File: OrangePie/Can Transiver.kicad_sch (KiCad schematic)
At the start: 0 parts

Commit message: Add usb hub and can tranceiver
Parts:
- added C18, C19: 100nF, Capacitor_SMD:C_0402_1005Metric, symbol Device:C_Small
- added R8: 10k, Resistor_SMD:R_0402_1005Metric, symbol Device:R_Small
- added U4: TJA1044GTK_3Z, Package_SON:HVSON-8-1EP_3x3mm_P0.65mm_EP1.6x2.4mm, symbol TJA1044GTK_3Z:TJA1044GTK_3Z
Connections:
- new net: R8.2, U4.8 (STB)
- new net +3V3: C19.2, U4.5 (VIO)
- new net +5V: C18.2, U4.3 (VCC)
- new net CAN_TR.RXD: U4.4 (RXD)
- new net CAN_TR.TXD: U4.1 (TXD)
- new net CAN_TR_OUT.+: U4.7 (CANH)
- new net CAN_TR_OUT.-: U4.6 (CANL)
- new net GND: C18.1, C19.1, R8.1, U4.2 (GND), U4.9 (EP)

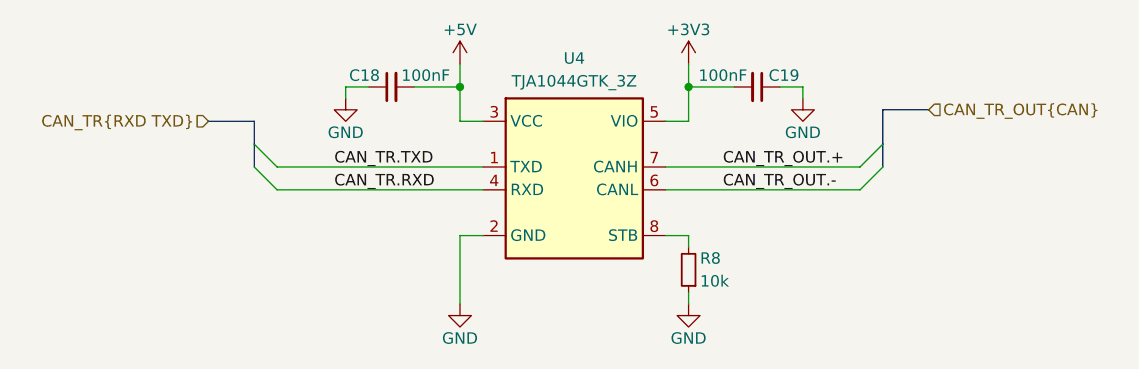
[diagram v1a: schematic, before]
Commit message: Update rest of schematic
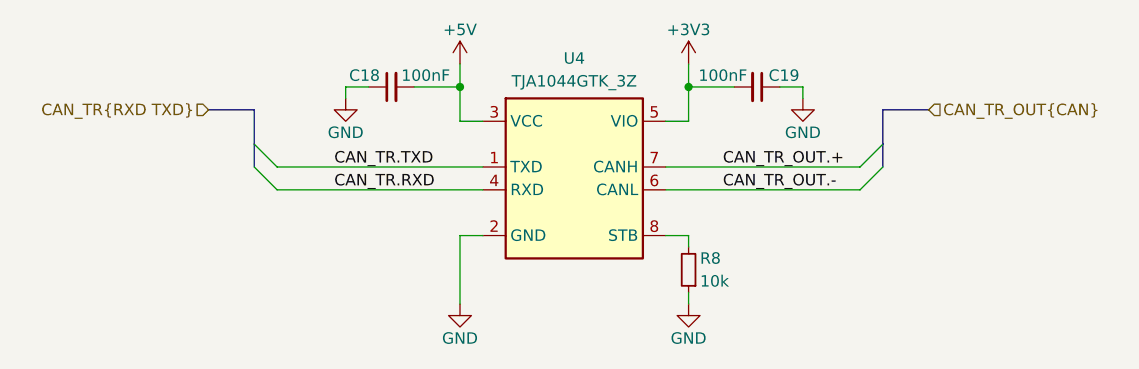
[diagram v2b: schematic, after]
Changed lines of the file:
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@@
 	(bus
 		(pts
-			(xy 96.52 95.25) (xy 101.6 95.25)
+			(xy 96.52 93.98) (xy 101.6 93.98)
 		)
 		(stroke
@@
 	(bus
 		(pts
-			(xy 101.6 95.25) (xy 101.6 97.79)
+			(xy 101.6 93.98) (xy 101.6 97.79)
 		)
 		(stroke
@@
 	(hierarchical_label "CAN_TR{RXD TXD}"
 		(shape input)
-		(at 96.52 95.25 180)
+		(at 96.52 93.98 180)
 		(fields_autoplaced yes)
 		(effects
@@
 					(unit 1)
 				)
+				(path "/3103c9de-f1ba-4d51-8bfc-798df1c75e2f/90c85cbd-0f83-4bab-9a58-f576d03aa82a"
+					(reference "#PWR032")
+					(unit 1)
+				)
 			)
 		)
@@
 					(unit 1)
 				)
+				(path "/3103c9de-f1ba-4d51-8bfc-798df1c75e2f/90c85cbd-0f83-4bab-9a58-f576d03aa82a"
+					(reference "R9")
+					(unit 1)
+				)
 			)
 		)
@@
 					(unit 1)
 				)
+				(path "/3103c9de-f1ba-4d51-8bfc-798df1c75e2f/90c85cbd-0f83-4bab-9a58-f576d03aa82a"
+					(reference "C20")
+					(unit 1)
+				)
 			)
 		)
@@
 					(unit 1)
 				)
+				(path "/3103c9de-f1ba-4d51-8bfc-798df1c75e2f/90c85cbd-0f83-4bab-9a58-f576d03aa82a"
+					(reference "#PWR033")
+					(unit 1)
+				)
 			)
 		)
@@
 					(unit 1)
 				)
+				(path "/3103c9de-f1ba-4d51-8bfc-798df1c75e2f/90c85cbd-0f83-4bab-9a58-f576d03aa82a"
+					(reference "#PWR037")
+					(unit 1)
+				)
 			)
 		)
@@
 				(path "/3103c9de-f1ba-4d51-8bfc-798df1c75e2f/4ef8679b-7d0c-4776-8ce3-817c4ec1763f"
 					(reference "U4")
+					(unit 1)
+				)
+				(path "/3103c9de-f1ba-4d51-8bfc-798df1c75e2f/90c85cbd-0f83-4bab-9a58-f576d03aa82a"
+					(reference "U5")
 					(unit 1)
 				)
@@
 					(unit 1)
 				)
+				(path "/3103c9de-f1ba-4d51-8bfc-798df1c75e2f/90c85cbd-0f83-4bab-9a58-f576d03aa82a"
+					(reference "#PWR035")
+					(unit 1)
+				)
 			)
 		)
@@
 					(unit 1)
 				)
+				(path "/3103c9de-f1ba-4d51-8bfc-798df1c75e2f/90c85cbd-0f83-4bab-9a58-f576d03aa82a"
+					(reference "#PWR036")
+					(unit 1)
+				)
 			)
 		)
@@
 				(path "/3103c9de-f1ba-4d51-8bfc-798df1c75e2f/4ef8679b-7d0c-4776-8ce3-817c4ec1763f"
 					(reference "#PWR028")
+					(unit 1)
+				)
+				(path "/3103c9de-f1ba-4d51-8bfc-798df1c75e2f/90c85cbd-0f83-4bab-9a58-f576d03aa82a"
+					(reference "#PWR034")
 					(unit 1)
 				)
@@
 					(unit 1)
 				)
+				(path "/3103c9de-f1ba-4d51-8bfc-798df1c75e2f/90c85cbd-0f83-4bab-9a58-f576d03aa82a"
+					(reference "C21")
+					(unit 1)
+				)

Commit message: Add CH340 debug
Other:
- company: (none) -> ModuCard System
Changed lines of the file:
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@@
 	(generator_version "8.0")
 	(paper "A4")
+	(title_block
+		(date "2025-02-10")
+		(rev "A")
+		(company "ModuCard System")
+	)
 	(bus_alias "CAN"
 		(members "+" "-")
@@
 	(label "CAN_TR.TXD"
 		(at 110.49 100.33 0)
+		(fields_autoplaced yes)
 		(effects
 			(font
@@
 	(label "CAN_TR_OUT.+"
 		(at 153.67 100.33 0)
+		(fields_autoplaced yes)
 		(effects
 			(font
@@
 	(label "CAN_TR.RXD"
 		(at 110.49 102.87 0)
+		(fields_autoplaced yes)
 		(effects
 			(font
@@
 	(label "CAN_TR_OUT.-"
 		(at 153.67 102.87 0)
+		(fields_autoplaced yes)
 		(effects
 			(font
